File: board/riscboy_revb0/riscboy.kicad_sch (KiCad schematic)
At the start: 74 parts

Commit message: More work on revb board schematic
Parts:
- removed D?: LED, symbol Device:LED
- removed J?: Conn_02x06_Odd_Even, symbol Connector_Generic:Conn_02x06_Odd_Even
- removed R?: 1k, symbol Device:R
- added D?: 19-337C_RSBHGHC, symbol riscboy:LED_RGB_oddeven
- added J?: 1827928-1 TE, symbol Connector_Generic:Conn_01x03
- added J?: NF, symbol Connector_Generic:Conn_02x04_Odd_Even
- added J?: 2.54mm head, symbol Connector_Generic:Conn_01x02
- added J?: NF, symbol Connector_Generic:Conn_01x05
- added R? (x2): 27, symbol Device:R
- added R?: 330, symbol Device:R
- added R?: 100, symbol Device:R
- added SW?: SW_SPDT, symbol Switch:SW_SPDT
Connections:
- net +BATT: now also R?.1, SW?.1 (A); no longer C?.1, U?.3 (VBAT)
- net BUTTON_A: now also U?.K5 (IOB_79); no longer U?.J4 (IOB_64)
- net BUTTON_B: now also U?.J7 (IOB_86); no longer U?.L3 (IOB_71)
- net BUTTON_X: now also U?.H7 (IOB_87); no longer U?.L4 (IOB_72)
- net BUTTON_Y: now also U?.K7 (IOB_89); no longer U?.K4 (IOB_73)
- net DPAD_D: now also U?.L7 (IOB_94); no longer U?.K5 (IOB_79)
- net DPAD_L: now also U?.L8 (IOB_103_CBSEL0); no longer U?.J7 (IOB_86)
- net DPAD_R: now also U?.H9 (IOB_104_CBSEL1); no longer U?.H7 (IOB_87)
- net DPAD_U: now also U?.J8 (IOB_91); no longer U?.J5 (IOB_78)
- net FPGA_CDONE: now also U?.29 (GPIO18), J?.3 (Pin_3); no longer U?.15 (GPIO12)
- net FPGA_FLASH_SCK: now also U?.18 (GPIO15), J?.4 (Pin_4); no longer U?.12 (GPIO9)
- net FPGA_FLASH_SD0: now also U?.27 (GPIO16), J?.6 (Pin_6); no longer U?.13 (GPIO10)
- net FPGA_FLASH_SD1: now also U?.28 (GPIO17), J?.8 (Pin_8); no longer U?.14 (GPIO11)
- net FPGA_FLASH_~CS~: now also U?.17 (GPIO14), J?.2 (Pin_2); no longer U?.11 (GPIO8)
- net FPGA_UART_TX: now also J?.5 (Pin_5)
- net FPGA_~RST~: now also U?.30 (GPIO19), J?.1 (Pin_1); no longer U?.16 (GPIO13)
- net GND: now also D?.3 (GK), D?.5 (BK), J?.1 (Pin_1), J?.1 (Pin_1), J?.5 (Pin_5), J?.7 (Pin_7)
- net LCD_LED: now also R?.2
- net MCU_UART_RX: now also U?.3 (GPIO1), J?.1 (Pin_1)
- net MCU_UART_TX: now also U?.2 (GPIO0), J?.2 (Pin_2)
- net SWCLK: now also J?.4 (Pin_4)
- net SWDIO: now also J?.3 (Pin_3)
- net VBUS: now also R?.1
- net CHARGE_LED: now reaches U?.1 (STAT)
- net CHARGE_LED: now also D?.1 (RK)
- new net: D?.6 (BA), R?.2
- new net: D?.2 (RA), R?.2
- new net: D?.4 (GA), R?.2
- new net +BATT_X: C?.1, J?.2 (Pin_2), J?.3 (Pin_3), SW?.2 (B), U?.3 (VBAT)
- new net FPGA_LED: R?.1
- new net FPGA_SPARE_IO0: U?.11 (GPIO8), U?.J4 (IOB_64)
- new net FPGA_SPARE_IO1: U?.12 (GPIO9), U?.L3 (IOB_71)
- new net FPGA_SPARE_IO2: U?.13 (GPIO10), U?.L4 (IOB_72)
- new net FPGA_SPARE_IO3: U?.14 (GPIO11), U?.K4 (IOB_73)
- new net FPGA_SPARE_IO4: U?.15 (GPIO12), U?.J5 (IOB_78)
- new net MCU_LED: R?.1
- no-connect marks 3 -> 5
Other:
- note added: "Just use a slide switch to switch the battery directly. A bit questionable, but the Chinese Gameboy thing gets away with it. It'll be fine for B0. At some point should revisit this to get a circuit that doesn't pass system current through the switch, and doesn't leak terribly."
- note added: "The case has a little opening in the black LCD surround, and there are two LEDs (red and green discrete) on the original board, which shine through this hole. Red is used for charging, green seems to just be a power indicator. Not sure how readable it will be to have three colours of LED like this (especially if you're colour blind :/ ) so the LEDs ought to be blink/blonked sparingly. LED params 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"
- note removed: "TODO LED"
- note removed: "TODO power switch?"
- moved on the sheet: C?, J?, L?, R?, SW?, U?

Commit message: Add speaker + stereo audio outputs. Starting to look vaguely plausible
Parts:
- added C? (x3): 4u7, symbol Device:C
- added C? (x2): 100n, symbol Device:C
- added J?: 2.5mm-3P-TRS, symbol Connector:AudioJack3
- added JP? (x2): cut/solder, symbol Jumper:Jumper_3_Bridged12
- added LS?: Speaker, symbol Device:Speaker
- added R? (x2): 100, symbol Device:R
- added R? (x2): 27, symbol Device:R
- added R? (x2): 330, symbol Device:R
- added U? (x3): 74LVC2G34, symbol riscboy:74LVC2G34
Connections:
- net +3V3: now also R?.1, C?.1, U?.5 (VCC)
- net +BATT: no longer R?.1
- net FPGA_ROOT_CLK: now also U?.B6 (IOT_198_GBIN0); no longer U?.K6 (IOB_82_GBIN4)
- net GND: now also C?.2, C?.2, C?.2, J?.S, R?.1, R?.1, U?.2 (GND)
- net SWCLK: now also JP?.3 (B)
- net SWDIO: now also JP?.3 (B)
- net USB_D+: no longer R?.2
- net USB_D-: no longer R?.2
- net SPEAKER_PWM+: now reaches U?.A1 (IOT_225)
- net SPEAKER_PWM+: now also U?.1
- net SPEAKER_PWM-: now reaches U?.B7 (IOT_197_GBIN1)
- net SPEAKER_PWM-: now also U?.3
- net STEREO_PWM_L: now reaches U?.L5 (IOB_81_GBIN5)
- net STEREO_PWM_L: now also R?.1
- new net: C?.1, C?.1, R?.2, R?.2 (x2)
- new net: C?.2, JP?.1 (A) (x2)
- new net: LS?.1, R?.2
- new net: LS?.2, R?.1
- new net: R?.2, U?.5
- new net: J?.R, JP?.2 (C)
- new net: J?.T, JP?.2 (C)
- new net: R?.1, U?.6
- new net STEREO_PWM_R: R?.1, U?.K6 (IOB_82_GBIN4)
- no-connect marks 5 -> 22
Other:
- note added: "LED params @ 20 mA: Vf (V), brightness (mcd) R (charge) 2.05 580 G (MCU) 2.9 1350 B (FPGA) 2.9 270 note this is just taking midpoint of min/max. So we probably want B @ 20 mA -> ~~20 R (!) G @ 4 mA -> ~~100 R R @ 10 mA -> ~~330 R (note +5V supply for R)"
- note added: "MIC23050 has an undervoltage lockout at 2.55V typical, with 100 mV hysteresis, and draws very little current in this state. We don't use +BATT directly, only through the regulators. This is a bit low for a Li-poly low cutout, but should help avoid turning our cell into a spicy pillow."
- note added: "TODO maybe should use NOT gates here (especially for the stereo, once we have a quiet supply) so that we don't immediately get a pop when the audio supply comes up."
- note removed: "The case has a little opening in the black LCD surround, and there are two LEDs (red and green discrete) on the original board, which shine through this hole. Red is used for charging, green seems to just be a power indicator. Not sure how readable it will be to have three colours of LED like this (especially if you're colour blind :/ ) so the LEDs ought to be blink/blonked sparingly. LED params 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"
- moved on the sheet: C?, D?, J?, L?, R?, SW?, U?, U?A, U?B, U?C, U?F, Y?

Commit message: Add separate audio supply
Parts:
- removed C?: 4u7, symbol Device:C
- removed J?: 2.54mm head, symbol Connector_Generic:Conn_01x02
- removed U? (x3): 74LVC2G34, symbol riscboy:74LVC2G34
- added C? (x4): 4u7, symbol Device:C
- added J?: 2.54mm, symbol Connector_Generic:Conn_01x03
- added R? (x2): 2k2, symbol Device:R
- added U? (x6): 74LVC2G04, symbol riscboy:74LVC2G04
- added U?: NCP115ASN330, symbol riscboy:NCP115ASN330
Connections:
- net +3V3: now also U?.3 (EN)
- net +BATT: now also C?.1, J?.3 (Pin_3), U?.1 (IN)
- net +BATT_X: now also J?.2 (Pin_2)
- net FPGA_LED: now also U?.B1 (IOL_2A)
- net GND: now also C?.1, C?.1, C?.2, C?.2, J?.1 (Pin_1), R?.1, R?.1, U?.2 (GND), U?.2 (GND), U?.2 (GND)
- net MCU_LED: now also U?.37 (GPIO25)
- net SPEAKER_PWM+: now also U?.1
- net SPEAKER_PWM-: now also U?.3
- net STEREO_PWM_L: now also U?.1; no longer R?.1
- net STEREO_PWM_R: now also U?.3; no longer R?.1
- net STEREO_L_DC: now reaches C?.1, C?.1, R?.2, R?.2
- net at C?.2, JP?.1 (A): now also R?.2 (x2)
- net at R?.2: now also U?.5
- net STEREO_R_DC: now reaches C?.1, C?.1, R?.2, R?.2
- net at R?.1: now also U?.6
- new net: R?.1, U?.6
- new net: R?.1, U?.5
- new net +3.3VA: C?.1, C?.2, C?.2, U?.5 (OUT), U?.5 (VCC), U?.5 (VCC)
- no-connect marks 22 -> 20
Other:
- note added: "A dual CMOS inverter is an H bridge, right? Right? No need for AC coupling cap -- just don't output any DC. Should be PWM'd at frequencies where the speaker appears inductive."
- note added: "Audio LDO enable is attached to 3V3 so that undervoltage lockout on the MIC23050 will also disable the LDO when the battery is discharged. The EN input on the NCP115 has a 0.9V threshold."
- note added: "Both BATT and BATT_X are exposed so that battery current can easily be measured."
- note added: "Buffer the PWM onto a quiet supply before filtering. Use inverters rather than buffers; iCE40 pulls pads high at reset, and we want the initial state to be low to minimise pop, then perform a software-controlled ramp. Trying to use existing passive values for the filter."
- note removed: "Just use a slide switch to switch the battery directly. A bit questionable, but the Chinese Gameboy thing gets away with it. It'll be fine for B0. At some point should revisit this to get a circuit that doesn't pass system current through the switch, and doesn't leak terribly."
- note removed: "TODO maybe should use NOT gates here (especially for the stereo, once we have a quiet supply) so that we don't immediately get a pop when the audio supply comes up."
- moved on the sheet: C?, D?, J?, JP?, L?, LS?, R?, SW?, U?, Y?

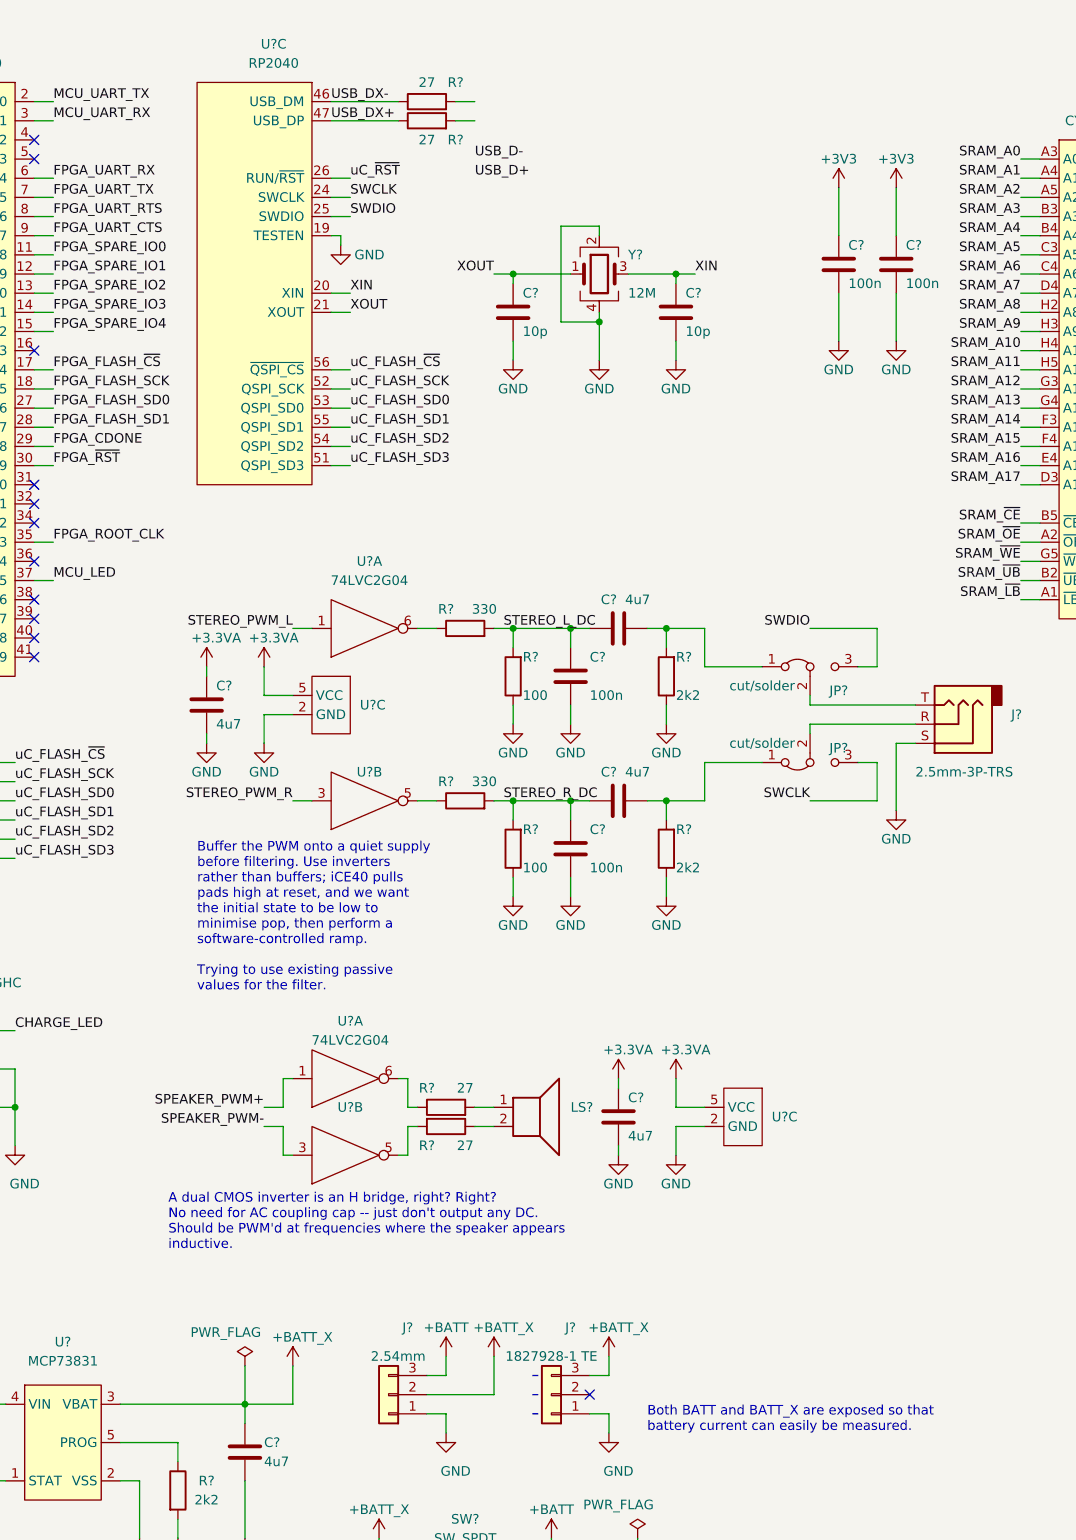
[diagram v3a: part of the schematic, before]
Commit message: ERC clean schematic, still needs some work/tidying though
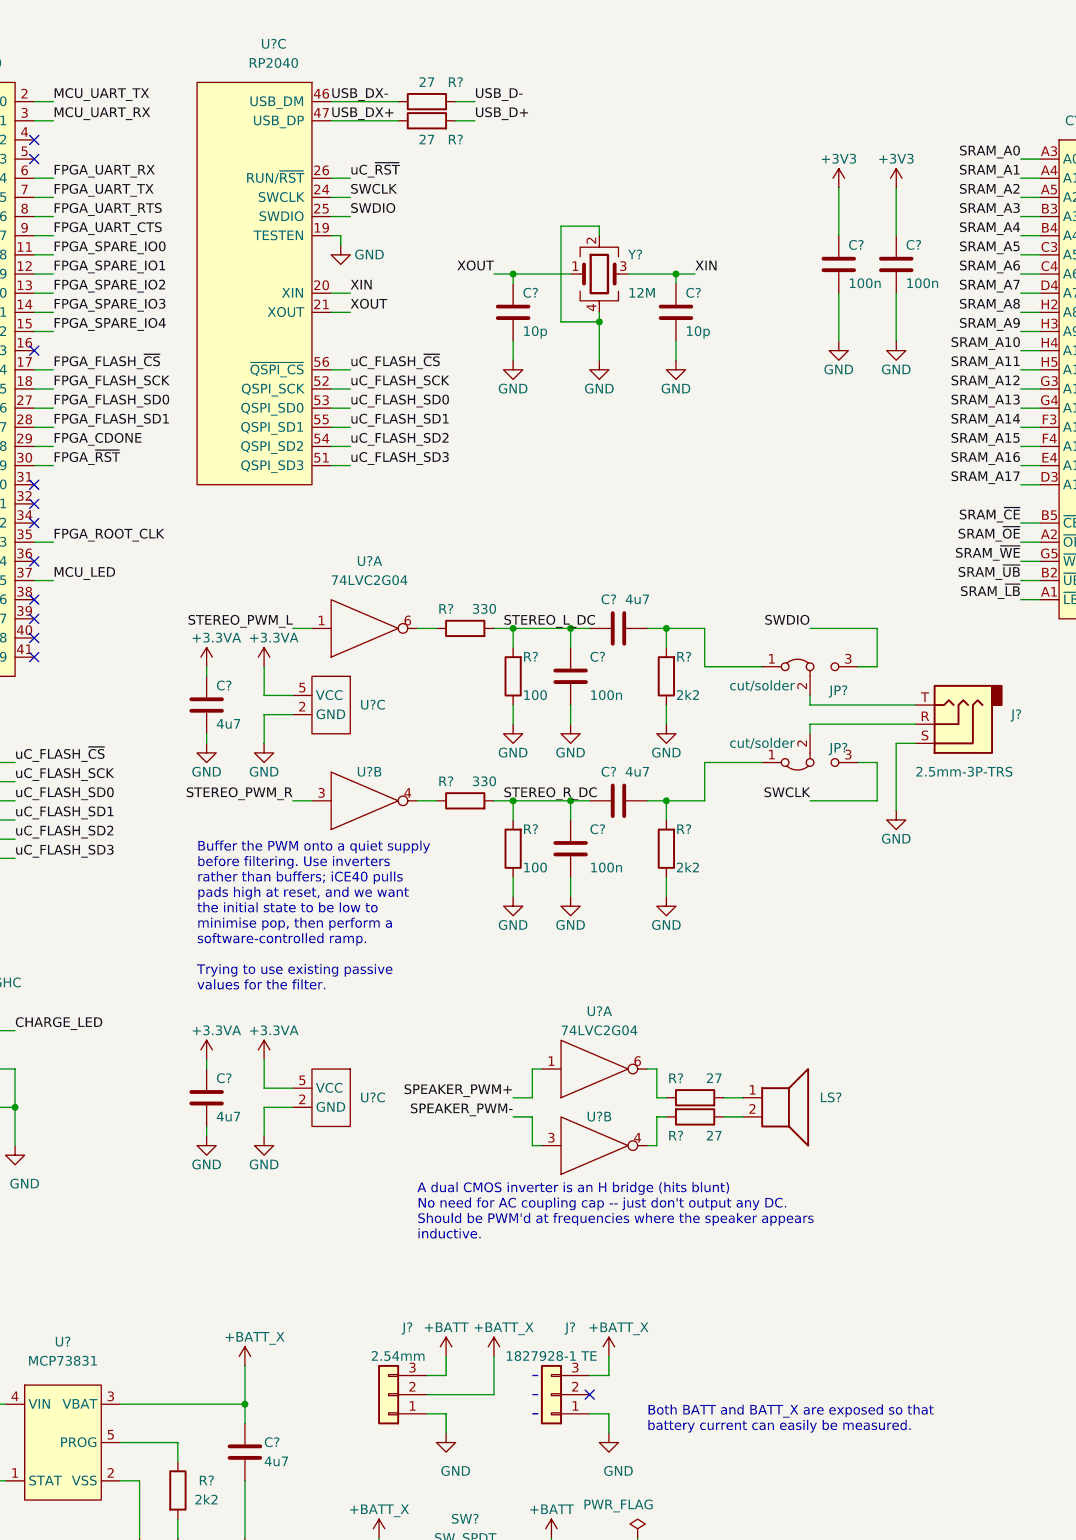
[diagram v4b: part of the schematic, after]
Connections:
- net USB_D+: now also R?.2
- net USB_D-: now also R?.2
- net at R?.2: now also U?.4; no longer U?.5
- net at R?.1: now also U?.4; no longer U?.5
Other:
- note added: "A dual CMOS inverter is an H bridge (hits blunt) No need for AC coupling cap -- just don't output any DC. Should be PWM'd at frequencies where the speaker appears inductive."
- note removed: "A dual CMOS inverter is an H bridge, right? Right? No need for AC coupling cap -- just don't output any DC. Should be PWM'd at frequencies where the speaker appears inductive."
- moved on the sheet: C?, LS?, R?, U?A, U?B, U?C

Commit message: Tweak debug headers, lots of schematic cleanup. Finally something worth turning into a PDF.
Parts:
- removed J?: NF, symbol Connector_Generic:Conn_01x05
- added J2: NF, symbol Connector_Generic:Conn_02x03_Odd_Even
- gave numbers to parts that had none: 96
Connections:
- net FPGA_CDONE: now also J7.1 (Pin_1); no longer J7.3 (Pin_3)
- net FPGA_UART_TX: now also J7.3 (Pin_3); no longer J7.5 (Pin_5)
- net FPGA_~RST~: now also J7.5 (Pin_5); no longer J7.1 (Pin_1)
- net GND: now also J2.5 (Pin_5)
- net SWCLK: now also J2.3 (Pin_3)
- net SWDIO: now also J2.1 (Pin_1)
- net uC_~RST~: now also J2.6 (Pin_6)
- net MCU_LED renamed uC_LED
- net MCU_UART_RX renamed uC_UART_RX
- net uC_UART_RX: now also J2.4 (Pin_4)
- net MCU_UART_TX renamed uC_UART_TX
- net uC_UART_TX: now also J2.2 (Pin_2)
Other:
- note added: "1V2 supply (FPGA + uC core)"
- note added: "3V3 Audio supply (high-PSRR LDO)"
- note added: "3V3 supply (FPGA + uC IO, LCD)"
- note added: "Audio"
- note added: "Battery spring contacts"
- note added: "Can jumper ~RST~ to GND"
- note added: "Configuration + User Flash"
- note added: "Cut + solder jumper points allow the TRS jack to be used as an external debug connector, to access RP2040 SWD without opening the case."
- note added: "Direct FPGA programming header"
- note added: "FPGA"
- note added: "Integrated lithium battery charger"
- note added: "LCD and Face Buttons"
- note added: "MIC23050 has an undervoltage lockout at 2.55V typical, with 100 mV hysteresis, and draws very little current in this state. We don't use +BATT directly, only through the regulators. This is a bit low for a Li-poly low cutout, but should help avoid turning an unprotected cell into a spicy pillow."
- note added: "Measurement header. Opening switch and measuring BATT_X->BATT gives system current."
- note added: "Microcontroller"
- note added: "Power Supply and Battery Management"
- note added: "Power supply notes: - VPP_FAST is NC if not using NVCM - VPP_2V5 can be 3V3 if not using NVCM - GNDPLL is tied to GND inside the FPGA - 10 uF value in datasheet is informative only; how brave are we feeling to save a BoM line?"
- note added: "SRAM for FPGA (4Mbit)"
- note added: "Switching battery directly (!)"
- note added: "TODO test points"
- note added: "Try to get brightness fairly consistent. LED params @ 20 mA: Vf (V), brightness (mcd) R 2.05 580 G 2.9 1350 B 2.9 270 note this is just taking midpoint of min/max. May need to tweak these -- I've set them fairly bright because they are shining through a tiny hole in the black LCD surround."
- note removed: "Both BATT and BATT_X are exposed so that battery current can easily be measured."
- note removed: "LED params @ 20 mA: Vf (V), brightness (mcd) R (charge) 2.05 580 G (MCU) 2.9 1350 B (FPGA) 2.9 270 note this is just taking midpoint of min/max. So we probably want B @ 20 mA -> ~~20 R (!) G @ 4 mA -> ~~100 R R @ 10 mA -> ~~330 R (note +5V supply for R)"
- note removed: "MIC23050 has an undervoltage lockout at 2.55V typical, with 100 mV hysteresis, and draws very little current in this state. We don't use +BATT directly, only through the regulators. This is a bit low for a Li-poly low cutout, but should help avoid turning our cell into a spicy pillow."
- note removed: "Optional Debug Header"
- note removed: "Power supply notes: - VPP_FAST is NC if not using NVMC - VPP_2V5 can be 3V3 if not using NVMC - GNDPLL is tied internally to the FPGA - 10 uF value in datasheet is informative only; how brave are we feeling to save a BoM line?"
- moved on the sheet: C14, C16, C19, C2, C22, C23, C24, C25, C26, C27, C28, C29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

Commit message: Add power testpoints, connect a few more spare FPGA IOs
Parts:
- removed SW1: SW_SPDT, symbol Switch:SW_SPDT
- added J? (x2): 2.54mm, symbol Connector_Generic:Conn_01x02
- added SW?: SW_SPDT, symbol Switch:SW_SPDT
- renumbered C24 to C?, C44 to C?, C26 to C?, C35 to C?, C18 to C?, C36 to C?, C14 to C?, C25 to C?, C9 to C?, C37 to C?, C17 to C?, C15 to C?, C38 to C?, C34 to C?, C2 to C?, C31 to C?, C27 to C?, C4 to C?, C10 to C?, C20 to C?, C21 to C?, C12 to C?, C5 to C?, C11 to C?, C16 to C?, C13 to C?, C40 to C?, C7 to C?, C32 to C?, C28 to C?, C22 to C?, C43 to C?, C30 to C?, C39 to C?, C19 to C?, C3 to C?, C29 to C?, C41 to C?, C1 to C?, C6 to C?, C8 to C?, C33 to C?, C42 to C?, C23 to C?, D1 to D?, J3 to J?, J4 to J?, J1 to J?, J6 to J?, J2 to J?, J7 to J?, J5 to J?, JP2 to JP?, JP1 to JP?, L1 to L?, L2 to L?, LS1 to LS?, R11 to R?, R10 to R?, R14 to R?, R13 to R?, R18 to R?, R15 to R?, R6 to R?, R8 to R?, R3 to R?, R1 to R?, R7 to R?, R16 to R?, R12 to R?, R2 to R?, R17 to R?, R4 to R?, R9 to R?, R5 to R?, SW7 to SW?, SW2 to SW?, SW8 to SW?, SW3 to SW?, SW5 to SW?, SW10 to SW?, SW9 to SW?, SW4 to SW?, SW6 to SW?, U1 to U?, U3 to U?, U6 to U?, U5 to U?, U10 to U?, U9 to U?, U7 to U?, U11 to U?, U8 to U?, U4 to U?, U2 to U?, Y1 to Y?
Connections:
- net +1V2: now also J?.1 (Pin_1)
- net +3V3: now also J?.1 (Pin_1)
- net +BATT: now also SW?.1 (A)
- net +BATT_X: now also SW?.2 (B)
- net BUTTON_A: now also U?.B2 (IOL_2B); no longer U?.K5 (IOB_79)
- net BUTTON_B: now also U?.C4 (IOL_4A); no longer U?.J7 (IOB_86)
- net BUTTON_X: now also U?.C3 (IOL_4B); no longer U?.H7 (IOB_87)
- net BUTTON_Y: now also U?.C2 (IOL_5A); no longer U?.K7 (IOB_89)
- net FPGA_CDONE: now also U?.32 (GPIO21); no longer U?.29 (GPIO18)
- net FPGA_FLASH_SCK: now also U?.29 (GPIO18); no longer U?.18 (GPIO15)
- net FPGA_FLASH_SD0: now also U?.30 (GPIO19); no longer U?.27 (GPIO16)
- net FPGA_FLASH_SD1: now also U?.31 (GPIO20); no longer U?.28 (GPIO17)
- net FPGA_FLASH_~CS~: now also U?.28 (GPIO17); no longer U?.17 (GPIO14)
- net FPGA_~RST~: now also U?.34 (GPIO22); no longer U?.30 (GPIO19)
- net GND: now also J?.2 (Pin_2), J?.2 (Pin_2)
- net FPGA_SPARE_IO5: now reaches U?.16 (GPIO13)
- net FPGA_SPARE_IO5: now also U?.K5 (IOB_79)
- new net FPGA_SPARE_IO6: U?.17 (GPIO14), U?.J7 (IOB_86)
- new net FPGA_SPARE_IO7: U?.18 (GPIO15), U?.H7 (IOB_87)
- no-connect marks 20 -> 14
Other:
- note added: "Through-hole testpoints"
- note removed: "Measurement header. Opening switch and measuring BATT_X->BATT gives system current."
- note removed: "TODO test points"
- moved on the sheet: J?
